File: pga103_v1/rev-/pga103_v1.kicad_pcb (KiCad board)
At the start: 2 copper layers, 38.1 x 25.4 mm, 29 parts, among them J1 RF_IN, J2 RF_OUT, U1 SPX3819M5-L-5-0, U2 PGA-103

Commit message: fixed silk screen for dimensions in V1
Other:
- board text added: "1.25{dblquote}"
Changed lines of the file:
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@@
     (effects (font (size 0.762 0.762) (thickness 0.1524) bold) (justify left bottom mirror))
   )
-  (gr_text "1.0{dblquote}" (at 114.3 120.65) (layer "B.SilkS")
+  (gr_text "1.25{dblquote}" (at 114.3 120.65) (layer "B.SilkS")
     (effects (font (size 1.016 1.016) (thickness 0.2032) bold) (justify bottom mirror))
   )

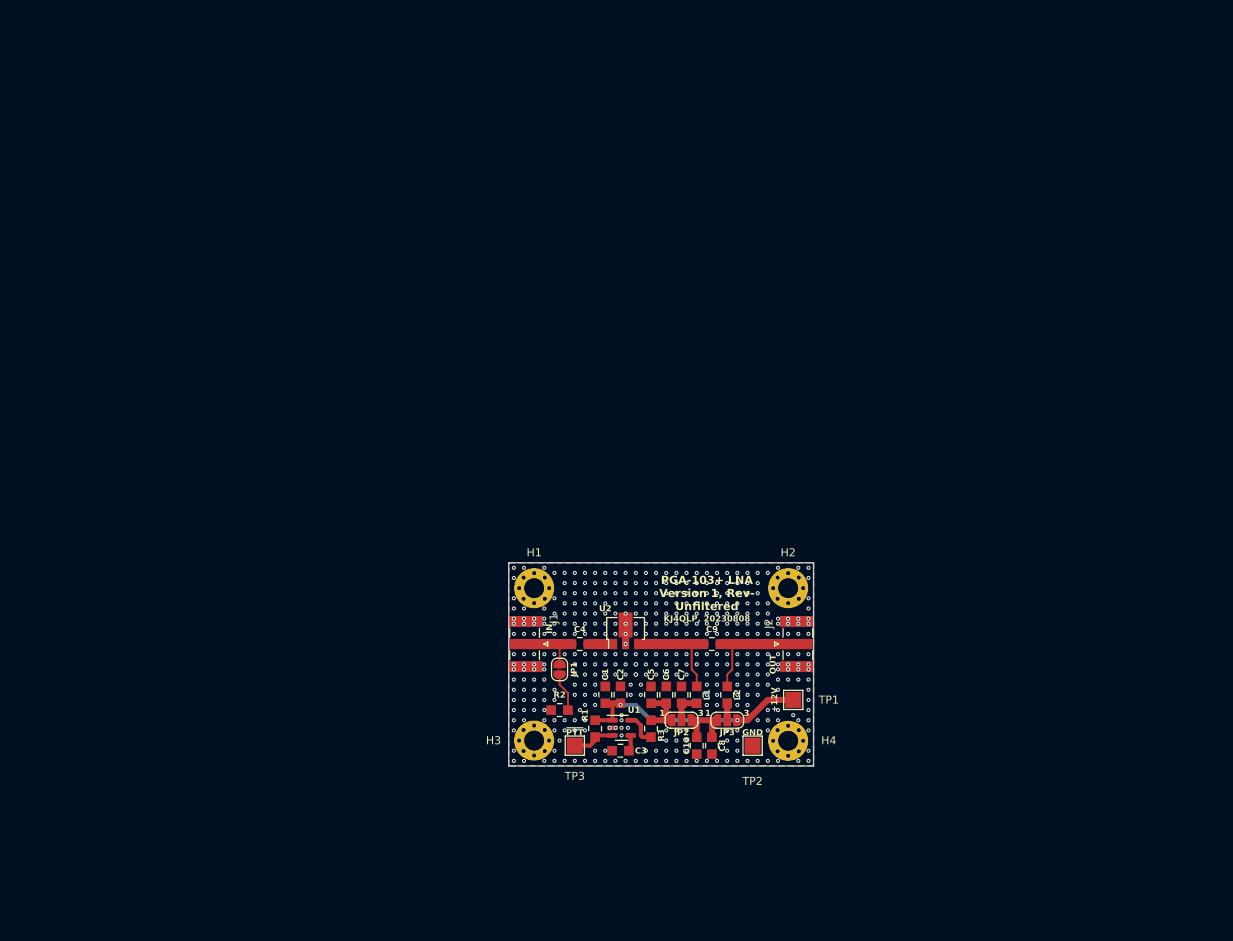
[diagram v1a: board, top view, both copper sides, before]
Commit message: updating board edge and adding shielding
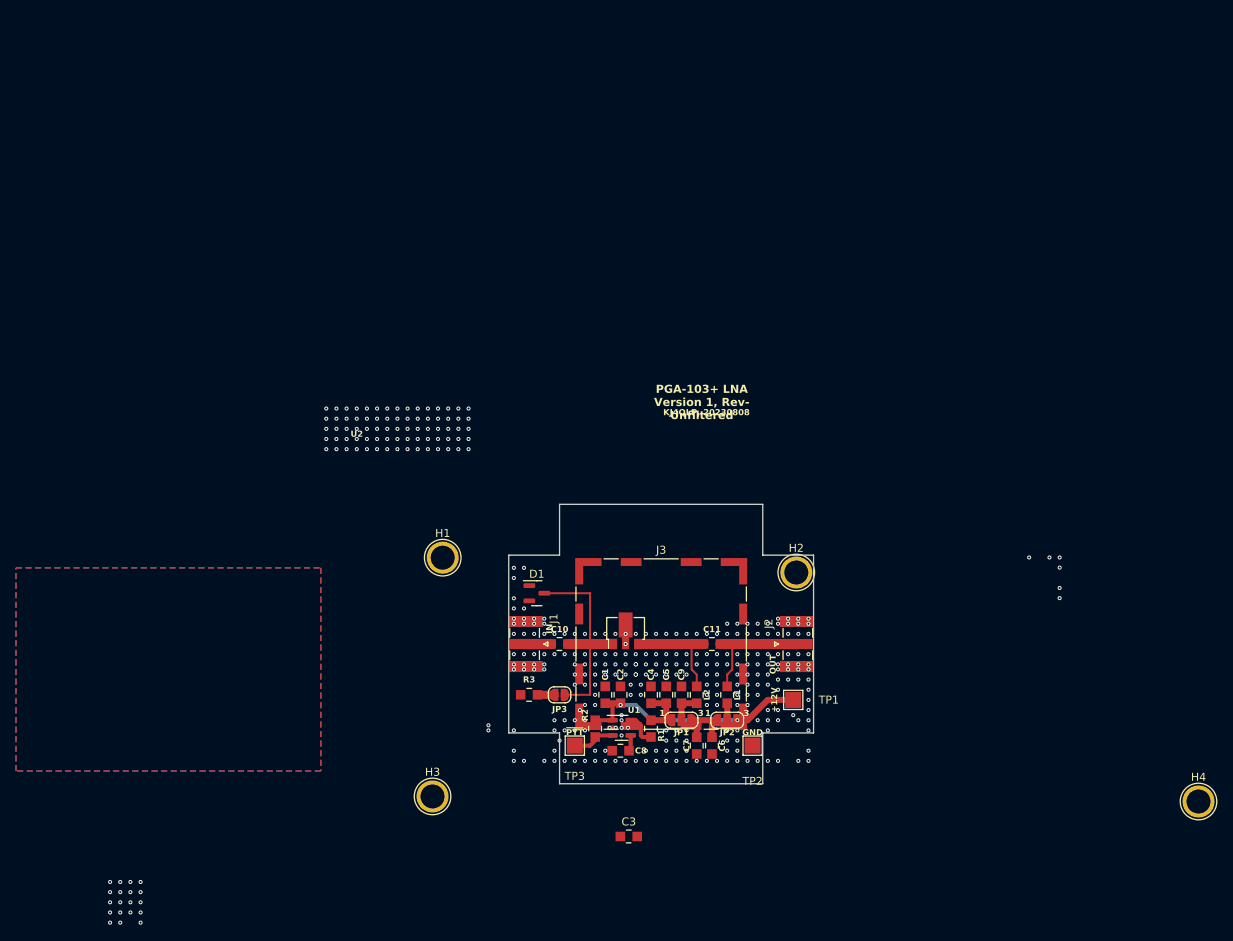
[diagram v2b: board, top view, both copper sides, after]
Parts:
- added C3: 0.1uF, digikey-footprints:0805, F.Cu at (110.3, 135.8)
- added D1: BAV99, Package_TO_SOT_SMD:SOT-23, F.Cu at (98.8, 105.4)
- added J3: RFShield_TwoPieces, RF_Shielding:Wuerth_36103205_20x20mm, F.Cu at (114.3, 111.8)
- C1: value 1uF -> 1.0uF
- C5: renamed from C6; value 0.1uF -> 1.0uF
- C6: renamed from C8; value 1uF -> 1.0uF
- H1, H2, H3, H4: footprint MountingHole:MountingHole_2.5mm_Pad_Via -> TestPoint:TestPoint_Plated_Hole_D3.0mm
- R1: renamed from R3; value 0 -> 10
- moved H4 51.9 mm to (181.5, 131.4)
- moved H3 14.5 mm to (85.7, 130.8)
- moved H1 12.0 mm to (87.0, 101.0)
- moved R3 4.26 mm to (97.8, 118.1)
- moved JP3 3.17 mm to (101.6, 118.1), turned to 180 degrees
- moved C10 2.54 mm to (101.6, 111.8)
- moved H2 2.20 mm to (131.2, 102.8)
- renumbered C4 to C10, C9 to C11, C5 to C4, C10 to C7, C3 to C8, C7 to C9, JP2 to JP1, JP3 to JP2, JP1 to JP3, L2 to L1, L1 to L2, R1 to R2, R2 to R3
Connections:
- C10 pad 2: Net-(C4-Pad2) -> Net-(JP3-A)
- JP3 pad 1: Net-(J1-In) -> Net-(JP3-A)
- U2 pad 1: Net-(C4-Pad2) -> Net-(JP3-A)
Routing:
- net Net-(JP3-A): track 0.00 -> 27.3 mm
- net Net-(J1-In): track 8.44 -> 3.38 mm
- net Net-(C4-Pad2): track 3.17 -> 0.00 mm
- net Net-(JP3-B): track 4.86 -> 2.11 mm
- net GND: vias 409 -> 357
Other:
- board size 38.1 x 25.4 mm -> 38.1 x 34.9 mm

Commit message: finalized V1 schematic and board
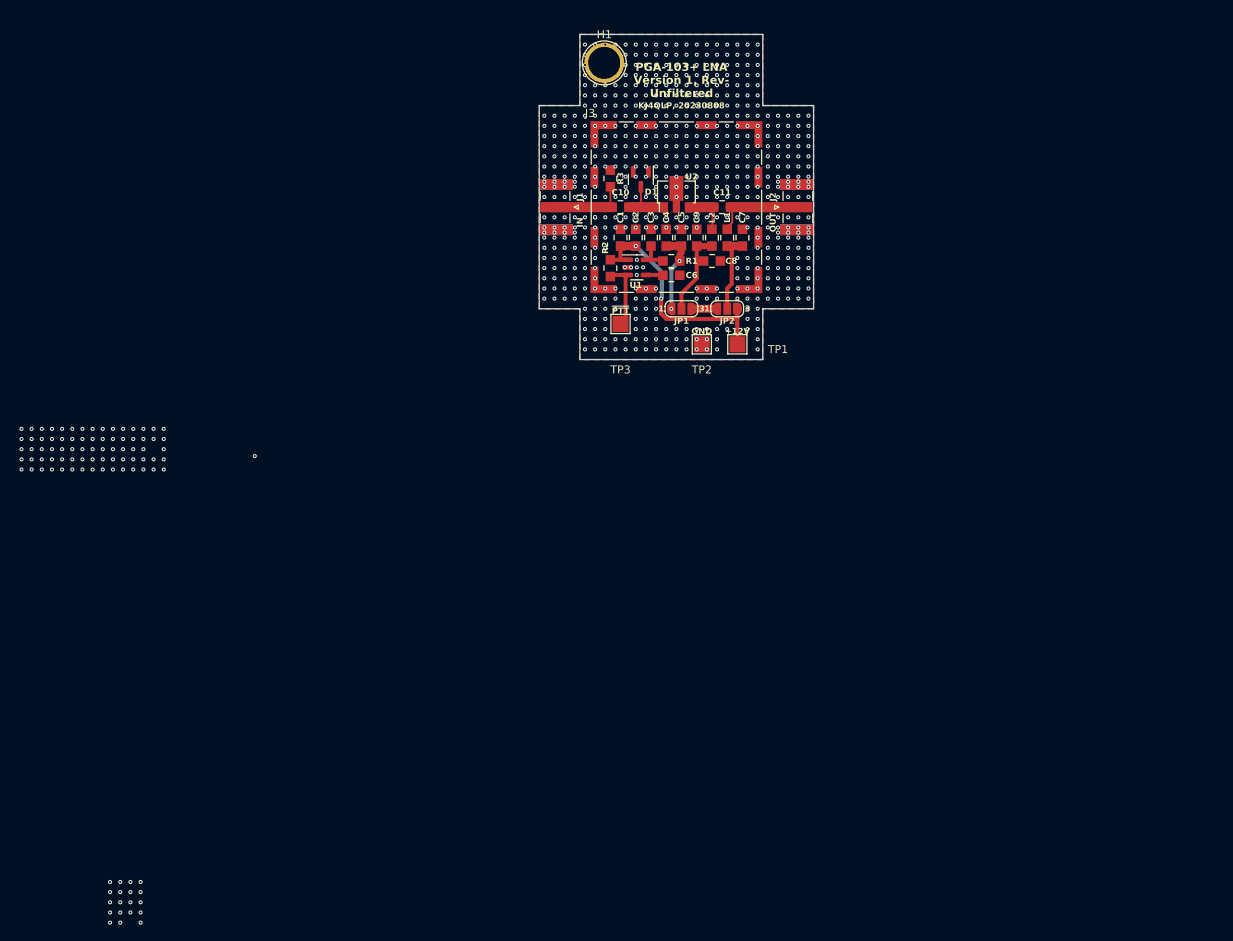
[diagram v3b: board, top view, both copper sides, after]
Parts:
- removed H2, H3, H4: Hole, TestPoint:TestPoint_Plated_Hole_D3.0mm
- removed JP3: SJO, Jumper:SolderJumper-2_P1.3mm_Open_RoundedPad1.0x1.5mm
- C10, C11, C9: value 18pF -> 1000pF
- C7: renamed from C6; value 1.0uF -> 1000pF
- H1: footprint TestPoint:TestPoint_Plated_Hole_D3.0mm -> TestPoint:TestPoint_Plated_Hole_D4.0mm
- moved C3 74.9 mm to (113.0, 61.0), turned to -90 degrees
- moved R3 65.3 mm to (108.0, 53.6), turned to 90 degrees
- moved H1 65.1 mm to (107.2, 39.1)
- moved C7 63.6 mm to (124.5, 61.0)
- moved C8 60.6 mm to (120.7, 63.9), turned to 180 degrees
- moved C6 59.8 mm to (115.6, 65.7), turned to 180 degrees
- moved R1 58.5 mm to (115.6, 63.9), turned to 0 degrees
- moved R2 57.6 mm to (108.0, 64.8)
- moved U1 57.6 mm to (111.3, 64.7)
- moved C1 57.2 mm to (109.2, 61.0)
- moved C2 57.2 mm to (111.1, 61.0)
- moved C4 57.2 mm to (114.9, 61.0)
- moved C5 57.2 mm to (116.8, 61.0)
- moved C9 57.2 mm to (118.7, 61.0)
- moved L2 57.2 mm to (120.7, 61.0)
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- renumbered C8 to C6, C7 to C8
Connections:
- C7 pad 1: GND -> Net-(JP2-C)
- C7 pad 2: Net-(JP1-B) -> GND
- C8 pad 2: Net-(JP1-B) -> Net-(JP1-C)
- J3 pad 1: unconnected-(J3-Shield-Pad1) -> GND
- R3 pad 1: Net-(JP3-B) -> Net-(J1-In)
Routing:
- net Net-(C10-Pad2): track 27.3 -> 7.30 mm
- net Net-(JP2-C): track 2.12 -> 10.2 mm
- net Net-(C11-Pad1): track 13.8 -> 6.07 mm
- net Net-(JP1-C): track 4.03 -> 11.5 mm
- net Net-(J1-In): track 3.38 -> 10.5 mm
- net Net-(JP1-B): track 8.57 -> 3.11 mm
- net +5V: track 6.54 -> 10.3 mm, vias 0 -> 2
- net Net-(J2-In): track 15.3 -> 11.6 mm
- net Net-(U1-EN): track 5.50 -> 8.75 mm
- net Net-(JP3-B): track 2.11 -> 0.00 mm
- net GND: vias 357 -> 696
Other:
- board size 38.1 x 34.9 mm -> 34.3 x 40.6 mm
- board text added: "JP1"
- board text removed: "JP3"

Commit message: forgot to save last commit.....
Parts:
- moved C10 1.91 mm to (111.1, 57.1)
- moved D1 1.27 mm to (110.5, 53.7)
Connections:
- D1 pad 3: Net-(C10-Pad2) -> Net-(J1-In)
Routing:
- net Net-(J1-In): track 10.5 -> 17.0 mm
- net Net-(C10-Pad2): track 7.30 -> 2.55 mm
- net GND: vias 696 -> 697
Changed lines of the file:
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@@
   )
   (footprint "digikey-footprints:0805" (layer "F.Cu")
-    (at 109.22 57.15)
+    (at 111.125 57.15)
     (property "Sheetfile" "pga103_v1.kicad_sch")
     (property "Sheetname" "")
@@
     (property "ki_keywords" "cap capacitor")
     (attr smd)
-    (fp_text reference "C10" (at 0 -1.84) (layer "F.SilkS")
+    (fp_text reference "C10" (at 0 -1.27) (layer "F.SilkS")
         (effects (font (size 0.762 0.762) (thickness 0.1524) bold))
     )
@@
     (property "ki_keywords" "mounting hole")
     (attr exclude_from_pos_files)
-    (fp_text reference "H1" (at 0 -3.548) (layer "F.SilkS")
+    (fp_text reference "H1" (at 0 -4.826) (layer "F.SilkS")
         (effects (font (size 1 1) (thickness 0.15)))
     )
@@
         (effects (font (size 1 1) (thickness 0.15)))
     )
-    (fp_text user "${REFERENCE}" (at 0 -3.55) (layer "F.Fab")
+    (fp_text user "${REFERENCE}" (at 0 -4.826) (layer "F.Fab")
         (effects (font (size 1 1) (thickness 0.15)))
     )
@@
   )
   (footprint "Package_TO_SOT_SMD:SOT-23" (layer "F.Cu")
-    (at 111.76 53.6725 -90)
+    (at 110.49 53.6725 -90)
     (descr "SOT, 3 Pin (https://www.jedec.org/system/files/docs/to-236h.pdf variant AB), generated with kicad-footprint-generator ipc_gullwing_generator.py")
     (tags "SOT TO_SOT_SMD")
@@
     (property "ki_keywords" "diode")
     (attr smd)
-    (fp_text reference "D1" (at 1.5725 -1.27 -180) (layer "F.SilkS")
+    (fp_text reference "D1" (at -2.2375 0 -180) (layer "F.SilkS")
         (effects (font (size 0.762 0.762) (thickness 0.1524) bold))
     )
@@
       (net 2 "GND") (pinfunction "A") (pintype "passive"))
     (pad "3" smd roundrect (at 0.9375 0 270) (size 1.475 0.6) (layers "F.Cu" "F.Paste" "F.Mask") (roundrect_rratio 0.25)
-      (net 9 "Net-(C10-Pad2)") (pinfunction "K") (pintype "passive"))
+      (net 5 "Net-(J1-In)") (pinfunction "K") (pintype "passive"))
     (model "${KICAD6_3DMODEL_DIR}/Package_TO_SOT_SMD.3dshapes/SOT-23.wrl"
       (offset (xyz 0 0 0))
@@
     (property "ki_keywords" "R res resistor")
     (attr smd)
-    (fp_text reference "R3" (at 0 1.27 90) (layer "F.SilkS")
+    (fp_text reference "R3" (at 2.125 0 180) (layer "F.SilkS")
         (effects (font (size 0.762 0.762) (thickness 0.1524) bold))
     )
@@
   )
   (footprint "Package_TO_SOT_SMD:SOT-89-3" (layer "F.Cu")
-    (at 116.205 55.245 90)
+    (at 116.205 55.2 90)
     (descr "SOT-89-3, http://ww1.microchip.com/downloads/en/DeviceDoc/3L_SOT-89_MB_C04-029C.pdf")
     (tags "SOT-89-3")
@@
     (effects (font (size 0.762 0.762) (thickness 0.1524) bold) (justify left bottom mirror))
   )
-  (gr_text "G:" (at 116.84 88.9) (layer "B.SilkS")
-    (effects (font (size 0.762 0.762) (thickness 0.1524) bold) (justify right mirror))
+  (gr_text "G:" (at 119.38 60.96) (layer "B.SilkS")
+    (effects (font (size 1.27 1.27) (thickness 0.2032)) (justify right mirror))
   )
   (gr_text "JP2" (at 114.3 46.355) (layer "B.SilkS")
@@
     (effects (font (size 1.016 1.016) (thickness 0.2032) bold) (justify bottom mirror))
   )
-  (gr_text "SN:" (at 116.84 92.71) (layer "B.SilkS")
-    (effects (font (size 0.762 0.762) (thickness 0.1524) bold) (justify right mirror))
+  (gr_text "SN:" (at 119.38 66.04) (layer "B.SilkS")
+    (effects (font (size 1.27 1.27) (thickness 0.2032)) (justify right mirror))
   )
   (gr_text "FALSE" (at 110.49 50.165) (layer "B.SilkS")
@@
     (effects (font (size 0.762 0.762) (thickness 0.1524) bold) (justify left bottom mirror))
   )
-  (gr_text "NF:" (at 116.7638 90.805) (layer "B.SilkS")
-    (effects (font (size 0.762 0.762) (thickness 0.1524) bold) (justify right mirror))
+  (gr_text "NF:" (at 119.3038 63.5) (layer "B.SilkS")
+    (effects (font (size 1.27 1.27) (thickness 0.2032)) (justify right mirror))
   )
   (gr_text "#2" (at 46.99 96.52) (layer "B.SilkS")
@@
     (effects (font (size 0.762 0.762) (thickness 0.1524) bold) (justify bottom))
   )
-  (gr_text "KJ4QLP, 20230808" (at 116.84 44.45) (layer "F.SilkS")
+  (gr_text "KJ4QLP, 20230808" (at 118.745 41.91) (layer "F.SilkS")
     (effects (font (size 0.762 0.762) (thickness 0.1524) bold))
   )
@@
     (effects (font (size 0.762 0.762) (thickness 0.1524) bold) (justify bottom))
   )
-  (gr_text "PGA-103+ LNA\nVersion 1, Rev-\nUnfiltered" (at 116.84 41.275) (layer "F.SilkS")
+  (gr_text "PGA-103+ LNA\nVersion 1, Rev-\nUnfiltered" (at 118.745 38.735) (layer "F.SilkS")
     (effects (font (size 1.016 1.016) (thickness 0.2032) bold))
   )
@@
     (height 27.305)
     (gr_text "1600.0000 mils" (at 75.685 55.88 90) (layer "Dwgs.User")
-      (effects (font (size 1 1) (thickness 0.15)))
-    )
-    (format (prefix "") (suffix "") (units 3) (units_format 1) (precision 4))
-    (style (thickness 0.15) (arrow_length 1.27) (text_position_mode 0) (extension_height 0.58642) (extension_offset 0.5) keep_text_aligned)
-  )
-  (dimension (type aligned) (layer "Dwgs.User")
-    (pts (xy 99.06 46.355) (xy 133.35 46.355))
-    (height -20.32)
-    (gr_text "1350.0000 mils" (at 116.205 24.885) (layer "Dwgs.User")
       (effects (font (size 1 1) (thickness 0.15)))
     )
@@
   (via (at 118.745 59.69) (size 0.508) (drill 0.254) (layers "F.Cu" "B.Cu") (free) (net 2))
   (via (at 103.505 64.77) (size 0.508) (drill 0.254) (layers "F.Cu" "B.Cu") (free) (net 2))
+  (via (at 116.205 57.15) (size 0.508) (drill 0.254) (layers "F.Cu" "B.Cu") (free) (net 2))
   (via (at 126.365 68.58) (size 0.508) (drill 0.254) (layers "F.Cu" "B.Cu") (free) (net 2))
   (via (at 126.365 39.37) (size 0.508) (drill 0.254) (layers "F.Cu" "B.Cu") (free) (net 2))
@@
   (via (at 122.555 50.8) (size 0.508) (drill 0.254) (layers "F.Cu" "B.Cu") (free) (net 2))
   (via (at 117.475 73.66) (size 0.508) (drill 0.254) (layers "F.Cu" "B.Cu") (free) (net 2))
-  (via (at 109.855 54.61) (size 0.508) (drill 0.254) (layers "F.Cu" "B.Cu") (free) (net 2))
+  (via (at 112.395 54.61) (size 0.508) (drill 0.254) (layers "F.Cu" "B.Cu") (free) (net 2))
   (via (at 128.905 50.8) (size 0.508) (drill 0.254) (layers "F.Cu" "B.Cu") (free) (net 2))
   (via (at 131.445 45.72) (size 0.508) (drill 0.254) (layers "F.Cu" "B.Cu") (free) (net 2))
@@
   (segment (start 116.84 67.945) (end 118.745 66.04) (width 0.508) (layer "F.Cu") (net 4))
   (segment (start 118.745 66.04) (end 118.745 64.135) (width 0.508) (layer "F.Cu") (net 4))
-  (segment (start 100.3475 57.15) (end 108.17 57.15) (width 1.27) (layer "F.Cu") (net 5))
+  (segment (start 110.49 54.61) (end 110.49 56.735) (width 0.254) (layer "F.Cu") (net 5))
+  (segment (start 100.3475 57.15) (end 110.075 57.15) (width 1.27) (layer "F.Cu") (net 5))
+  (segment (start 108.17 57.15) (end 110.075 57.15) (width 0.254) (layer "F.Cu") (net 5))
   (segment (start 107.95 54.61) (end 107.95 56.93) (width 0.254) (layer "F.Cu") (net 5))
+  (segment (start 110.49 56.735) (end 110.075 57.15) (width 0.254) (layer "F.Cu") (net 5))
   (segment (start 107.95 56.93) (end 108.17 57.15) (width 0.254) (layer "F.Cu") (net 5))
   (segment (start 116.62 63.085) (end 116.84 62.865) (width 0.762) (layer "F.Cu") (net 6))
@@
   (segment (start 123.19 59.055) (end 123.19 57.37) (width 0.254) (layer "F.Cu") (net 8))
   (segment (start 122.555 59.69) (end 123.19 59.055) (width 0.254) (layer "F.Cu") (net 8))
-  (segment (start 111.76 57.15) (end 114.3 57.15) (width 1.27) (layer "F.Cu") (net 9))
+  (segment (start 112.175 57.15) (end 114.3 57.15) (width 1.27) (layer "F.Cu") (net 9))
   (segment (start 114.66 57.15) (end 114.705 57.195) (width 0.508) (layer "F.Cu") (net 9))
-  (segment (start 110.27 57.15) (end 111.76 57.15) (width 1.27) (layer "F.Cu") (net 9))
   (segment (start 114.3 57.15) (end 114.66 57.15) (width 0.508) (layer "F.Cu") (net 9))
-  (segment (start 110.49 56.93) (end 110.27 57.15) (width 0.254) (layer "F.Cu") (net 9))
-  (segment (start 111.76 54.61) (end 111.76 57.15) (width 0.254) (layer "F.Cu") (net 9))
   (segment (start 124.46 62.01) (end 122.555 62.01) (width 1.016) (layer "F.Cu") (net 10))
   (segment (start 123.117 66.748) (end 122.555 67.31) (width 0.508) (layer "F.Cu") (net 10))
@@
     (polygon
       (pts
-        (xy 109.855 88.265)
-        (xy 116.84 88.265)
-        (xy 116.84 89.535)
-        (xy 109.855 89.535)
+        (xy 111.76 59.69)
+        (xy 119.38 59.69)
+        (xy 119.38 61.595)
+        (xy 111.76 61.595)
       )
     )
@@
     (polygon
       (pts
-        (xy 116.84 90.17)
-        (xy 109.855 90.17)
-        (xy 109.855 91.44)
-        (xy 116.84 91.44)
+        (xy 119.38 62.23)
+        (xy 111.76 62.23)
+        (xy 111.76 64.135)
+        (xy 119.38 64.135)
       )
     )
@@
     (polygon
       (pts
-        (xy 116.84 93.345)
-        (xy 109.855 93.345)
-        (xy 109.855 92.075)
-        (xy 116.84 92.075)
+        (xy 119.38 66.675)
+        (xy 111.76 66.675)
+        (xy 111.76 64.77)
+        (xy 119.38 64.77)
       )
     )
